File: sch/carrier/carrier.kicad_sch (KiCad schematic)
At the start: 0 parts

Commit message: get git committed
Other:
- sheet Battery system (revised) ports: added VBUS; removed none
- sheet Connectors ports: added VBUS_CHARGE; removed none
- note added: "IGNORE THIS SHEET, in a later revision might a low power microcontroller to the board to manage general control"
- note added: "Outputs: - Battery Monitor"
- note added: "Provides 1.8 and 3.3v power - i really cba to also regulate that"
- note added: "Snap off board for the display side- outputs are a 40 pin ZIF and a 8 pin ZIF (ffc's)"
- note added: "TODO: finish battery monitor and connect to pi GPIO."
- note removed: "Display board is meant to be a little snap off board section for the display section"
- note removed: "IGNORE THIS SHEET, in a later revision might a low power microcontroller to the board to manage RTC and power (software shutdowns, powerup and all that jazz) Thinking could use a STM microcontroller since they are common and ARM architecture"
- note removed: "Outputs: - I2C for battery monitor Inputs: - 5V power to battery charging TODO: route I2C to pi"
- note removed: "TODO: DPAD CONNECTIONS"
- note removed: "TODO: finish battery charger circuit TODO: finish battery monitor and connect to pi GPIO."

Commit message: aaaaaaaaaaaaaaaa
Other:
- sheet Battery system (revised) renamed Battery Charger
- added sheet Battery (battery.kicad_sch)
- sheet Battery Charger ports: added BATT, CHRG; removed FUEL_SCL, FUEL_SDA, VBUS
- note removed: "POTENTIAL EDIT: we should probably get rid of this, 1.8v logic from the pi is fine because we are not using it in load heavy applications, but if buck to 3.3v on our own thingy we should be able to make it more efficent (otherwise we are boosting for the pi to then buck)"
- note removed: "Provides 1.8 and 3.3v power - i really cba to also regulate that"
- note removed: "TODO: add the Start, Select and Backlight buttons"

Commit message: changes and carrier backups
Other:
- sheet Connectors ports: added +5v; removed none
- note added: "Connectors: - SD CARD - SPI DISPLAY"
- note removed: "INCOMPLETE"
- note removed: "connectors: - SD CARD - SPI DISPLAY"
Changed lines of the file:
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@@
     (comment 1 "https://www.github.com/cinnamondev/gamepithing")
   )
+  (wire (pts (xy 63.5 104.775) (xy 69.85 104.775))
+    (stroke (width 0) (type solid) (color 0 0 0 0))
+  )
   (wire (pts (xy 114.3 63.5) (xy 127 63.5))
     (stroke (width 0) (type solid) (color 0 0 0 0))
@@
     (stroke (width 0) (type solid) (color 0 0 0 0))
   )
-  (wire (pts (xy 149.86 50.165) (xy 149.86 57.15))
-    (stroke (width 0) (type solid) (color 0 0 0 0))
-  )
-  (wire (pts (xy 152.4 50.165) (xy 152.4 57.15))
-    (stroke (width 0) (type solid) (color 0 0 0 0))
-  )
-  (wire (pts (xy 154.94 50.165) (xy 154.94 57.15))
+  (wire (pts (xy 149.86 50.8) (xy 149.86 57.15))
+    (stroke (width 0) (type solid) (color 0 0 0 0))
+  )
+  (wire (pts (xy 152.4 53.34) (xy 152.4 57.15))
+    (stroke (width 0) (type solid) (color 0 0 0 0))
+  )
+  (wire (pts (xy 154.94 55.88) (xy 154.94 57.15))
+    (stroke (width 0) (type solid) (color 0 0 0 0))
+  )
+  (wire (pts (xy 159.385 50.8) (xy 149.86 50.8))
+    (stroke (width 0) (type solid) (color 0 0 0 0))
+  )
+  (wire (pts (xy 159.385 53.34) (xy 152.4 53.34))
+    (stroke (width 0) (type solid) (color 0 0 0 0))
+  )
+  (wire (pts (xy 159.385 55.88) (xy 154.94 55.88))
     (stroke (width 0) (type solid) (color 0 0 0 0))
   )
@@
   )
   (wire (pts (xy 222.25 116.205) (xy 196.85 116.205))
+    (stroke (width 0) (type solid) (color 0 0 0 0))
+  )
+  (wire (pts (xy 234.95 59.055) (xy 239.395 59.055))
     (stroke (width 0) (type solid) (color 0 0 0 0))
   )
@@
     (effects (font (size 1.27 1.27)) (justify left bottom))
   )
-  (text "connectors:\n- SD CARD\n- SPI DISPLAY" (at 160.02 75.565 180)
-    (effects (font (size 1.27 1.27)) (justify right bottom))
+  (text "Connectors:\n	- SD CARD\n	- SPI DISPLAY" (at 146.05 76.2 0)
+    (effects (font (size 1.27 1.27)) (justify left bottom))
   )
   (text "Outputs:\n	- Battery Monitor" (at 165.735 130.81 0)
@@
     (effects (font (size 1.27 1.27)) (justify left bottom))
   )
-  (text "INCOMPLETE" (at 201.93 93.98 0)
-    (effects (font (size 1.27 1.27)) (justify left bottom))
-  )
-  (label "+3.3v" (at 64.135 103.505 0)
-    (effects (font (size 1.27 1.27)) (justify left bottom))
-  )
-  (label "+1.8v" (at 149.86 50.165 270)
-    (effects (font (size 1.27 1.27)) (justify right bottom))
-  )
-  (label "+3.3v" (at 152.4 50.165 270)
-    (effects (font (size 1.27 1.27)) (justify right bottom))
-  )
-  (label "+5v" (at 154.94 50.165 270)
+  (label "+3.3v" (at 63.5 104.775 0)
+    (effects (font (size 1.27 1.27)) (justify left bottom))
+  )
+  (label "+1.8v" (at 159.385 50.8 180)
+    (effects (font (size 1.27 1.27)) (justify right bottom))
+  )
+  (label "+3.3v" (at 159.385 53.34 180)
+    (effects (font (size 1.27 1.27)) (justify right bottom))
+  )
+  (label "+5v" (at 159.385 55.88 180)
     (effects (font (size 1.27 1.27)) (justify right bottom))
   )
@@
     (effects (font (size 1.27 1.27)) (justify right bottom))
   )
+  (label "+5v" (at 239.395 59.055 180)
+    (effects (font (size 1.27 1.27)) (justify right bottom))
+  )
   (sheet (at 107.95 114.3) (size 38.1 31.75) (fields_autoplaced)
     (stroke (width 0.0006) (type solid) (color 0 0 0 0))
@@
       (effects (font (size 1.27 1.27)) (justify left top))
     )
-    (pin "FUEL_SDA" bidirectional (at 119.38 114.3 90)
+    (pin "FUEL_SDA" bidirectional (at 146.05 122.4915 0)
       (effects (font (size 1.27 1.27)) (justify right))
     )
@@
       (effects (font (size 1.27 1.27)) (justify left))
     )
-  )
+    (pin "+5v" input (at 234.95 59.055 0)
+      (effects (font (size 1.27 1.27)) (justify right))
+    )
+  )

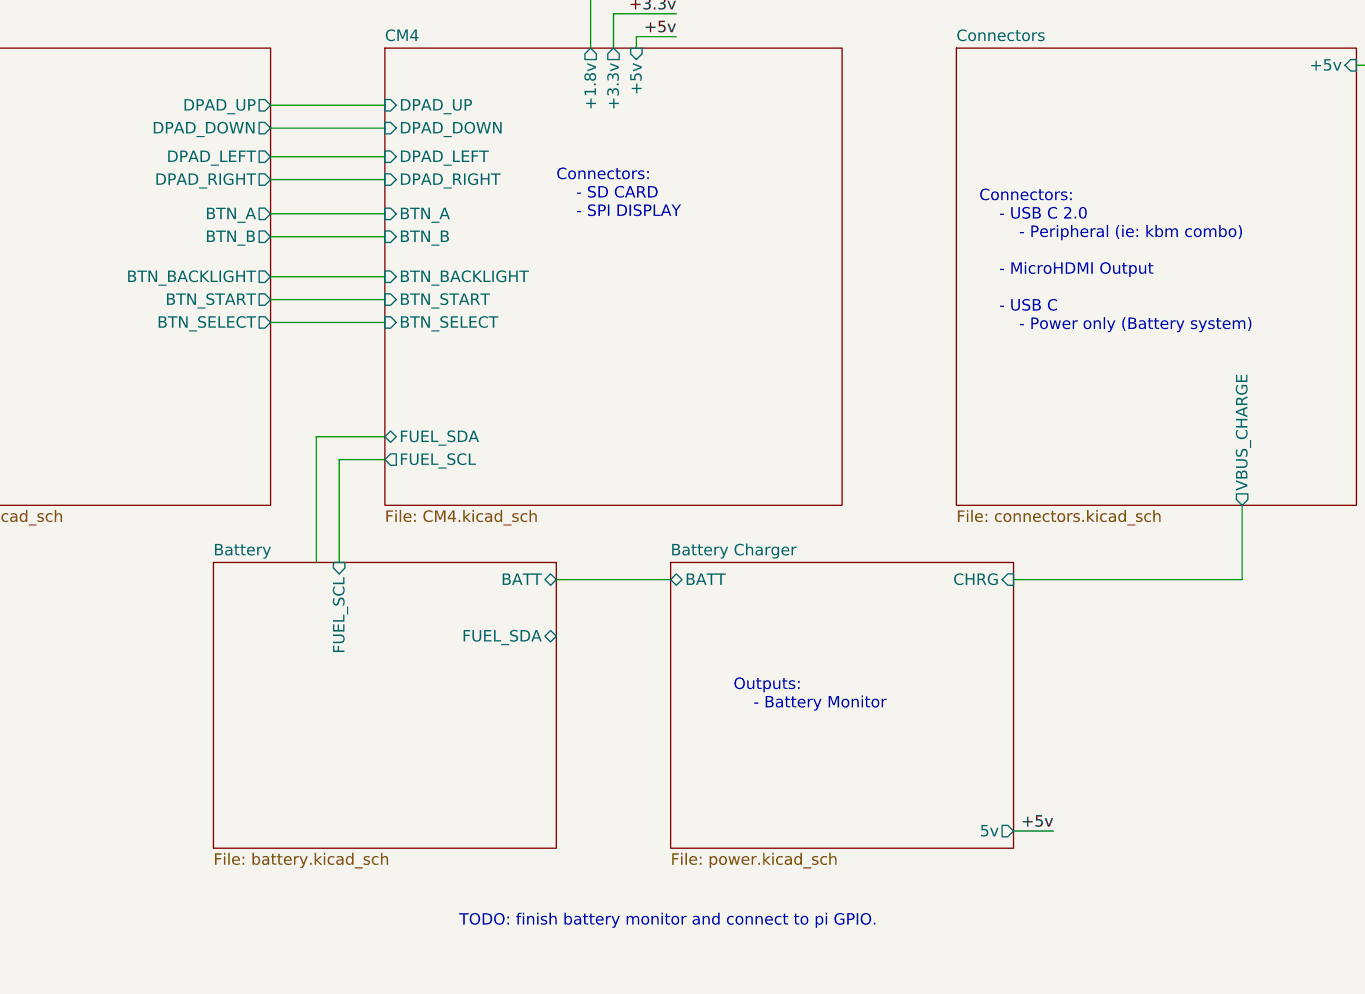
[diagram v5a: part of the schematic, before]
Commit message: add speaker and charger
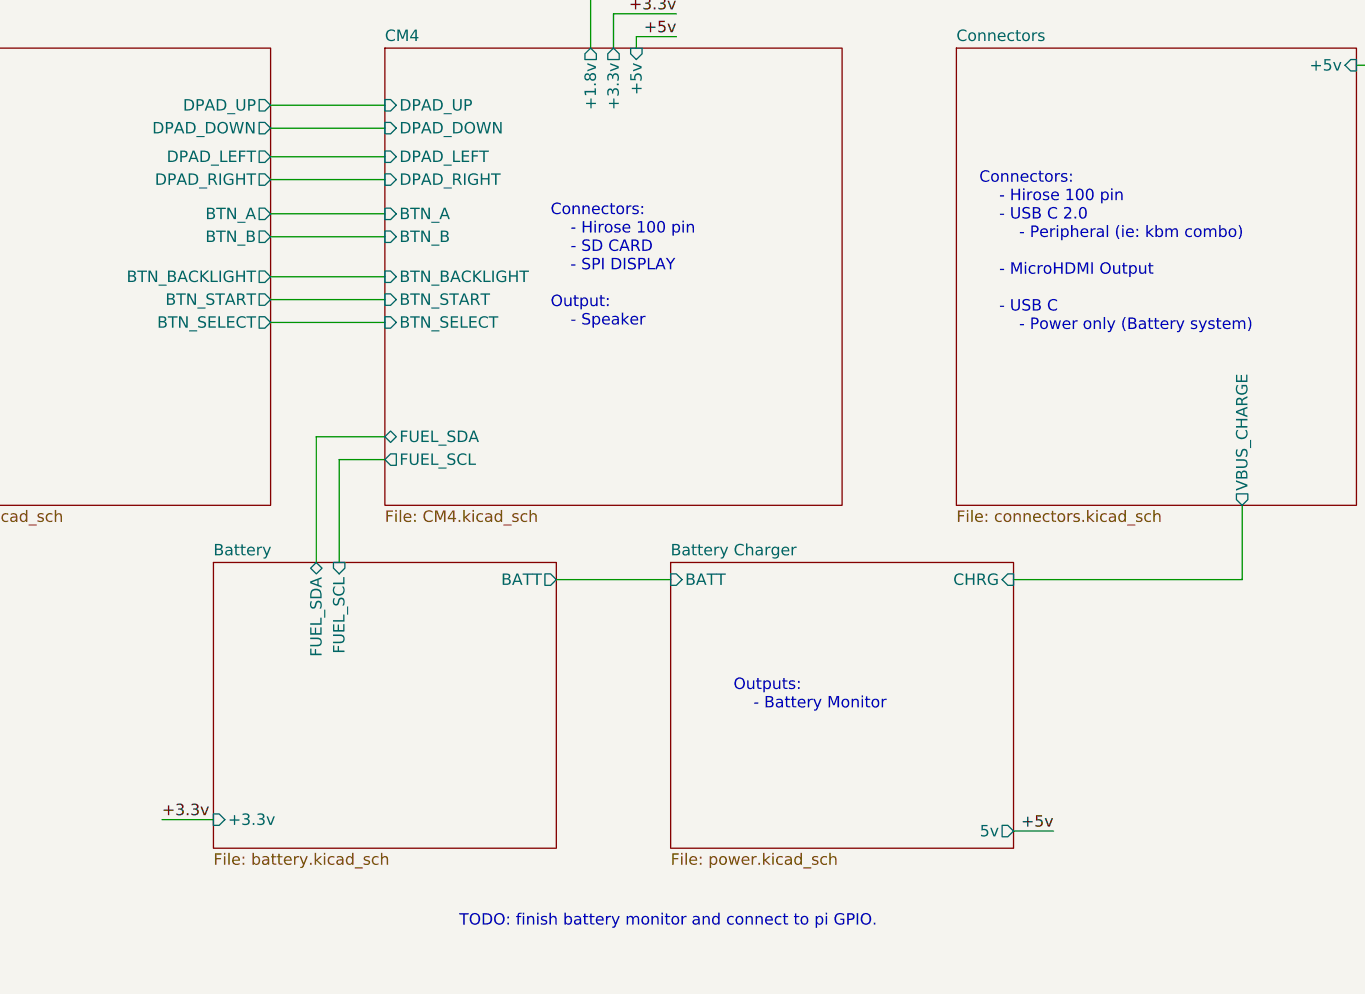
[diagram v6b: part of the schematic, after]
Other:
- sheet Battery ports: added +3.3v; removed none
- note added: "Connectors: - Hirose 100 pin - SD CARD - SPI DISPLAY Output: - Speaker"
- note added: "Connectors: - Hirose 100 pin - USB C 2.0 - Peripheral (ie: kbm combo) - MicroHDMI Output - USB C - Power only (Battery system)"
- note removed: "Connectors: - SD CARD - SPI DISPLAY"
- note removed: "Connectors: - USB C 2.0 - Peripheral (ie: kbm combo) - MicroHDMI Output - USB C - Power only (Battery system)"

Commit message: adsasdas
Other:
- sheet Buttons ports: added GLOBAL_EN; removed none
- sheet CM4 ports: added GLOBAL_EN; removed none
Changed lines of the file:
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@@
+    (stroke (width 0) (type solid) (color 0 0 0 0))
+  )
+  (wire (pts (xy 114.3 90.805) (xy 127 90.805))
     (stroke (width 0) (type solid) (color 0 0 0 0))
   )
@@
       (effects (font (size 1.27 1.27)) (justify right))
     )
+    (pin "GLOBAL_EN" input (at 114.3 90.805 0)
+      (effects (font (size 1.27 1.27)) (justify right))
+    )
   )
   (sheet (at 127 57.15) (size 50.8 50.8) (fields_autoplaced)
@@
     )
     (pin "FUEL_SCL" output (at 127 102.87 180)
+      (effects (font (size 1.27 1.27)) (justify left))
+    )
+    (pin "GLOBAL_EN" output (at 127 90.805 180)
       (effects (font (size 1.27 1.27)) (justify left))
     )
@@
       (reference "#PWR?") (unit 1) (value "GND") (footprint "")
     )
+    (path "/59fee1d9-7f44-408e-bd4e-36f39b8a6086/783a3c30-74e9-4ffd-8738-dbaee803b9d5"
+      (reference "#PWR?") (unit 1) (value "GND") (footprint "")
+    )
     (path "/8d0ae364-2b30-4b7c-813a-81b59cbe3cd0/7f4364c5-480f-4855-9f42-7cecbcfe99bd"
       (reference "#PWR?") (unit 1) (value "GND") (footprint "")
@@
       (reference "SW7") (unit 1) (value "SKRBAAE010") (footprint "eec:SKRBAAE010")
     )
+    (path "/59fee1d9-7f44-408e-bd4e-36f39b8a6086/1adb314a-0b8a-46c3-828a-e864cbaea687"
+      (reference "SW?") (unit 1) (value "SW_DIP_x04") (footprint "")
+    )
     (path "/59fee1d9-7f44-408e-bd4e-36f39b8a6086/5e1816fb-a04e-41a0-bdc2-371c4835f482"
       (reference "SW?") (unit 1) (value "SKRBAAE010") (footprint "eec:SKRBAAE010")
     )
-    (path "/59fee1d9-7f44-408e-bd4e-36f39b8a6086/65f9f988-f511-430a-b1c0-2814c302c06a"
-      (reference "SW?") (unit 1) (value "DTSM31NV") (footprint "")
-    )
     (path "/59fee1d9-7f44-408e-bd4e-36f39b8a6086/abd44681-3056-4284-a0b4-82e2ecb66505"
       (reference "SW?") (unit 1) (value "SKRBAAE010") (footprint "eec:SKRBAAE010")
@@
       (reference "TP?") (unit 1) (value "MOSI") (footprint "")
     )
+    (path "/59fee1d9-7f44-408e-bd4e-36f39b8a6086/33ed9fb8-80e0-4083-8d51-bfbaedbd44d8"
+      (reference "TP?") (unit 1) (value "STR") (footprint "TestPoint:TestPoint_Pad_2.0x2.0mm")
+    )
     (path "/95ef1699-d890-4da8-941a-b0ab341c2e25/35ca3d1c-30b3-42ec-812a-d9b4b971c6ce"
       (reference "TP?") (unit 1) (value "SCLK") (footprint "")
     )
+    (path "/59fee1d9-7f44-408e-bd4e-36f39b8a6086/62d72acd-259b-4860-a644-b0e9b8e94683"
+      (reference "TP?") (unit 1) (value "SEL") (footprint "TestPoint:TestPoint_Pad_2.0x2.0mm")
+    )
     (path "/19c5e008-dc4a-4080-a2ed-5cdad03792a4/83e1088b-b931-4ce2-bd34-5846d9180d04"
       (reference "TP?") (unit 1) (value "MISO") (footprint "")
@@
       (reference "TP?") (unit 1) (value "GND") (footprint "TestPoint:TestPoint_Pad_2.0x2.0mm")
     )
+    (path "/59fee1d9-7f44-408e-bd4e-36f39b8a6086/dbf5fcec-d94c-45af-b88d-3b5262f38dc0"
+      (reference "TP?") (unit 1) (value "BKL") (footprint "TestPoint:TestPoint_Pad_2.0x2.0mm")
+    )
     (path "/19c5e008-dc4a-4080-a2ed-5cdad03792a4/dc5e3a99-5725-46a6-9637-3836bee07890"
